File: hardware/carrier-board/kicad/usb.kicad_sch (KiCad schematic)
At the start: 0 parts

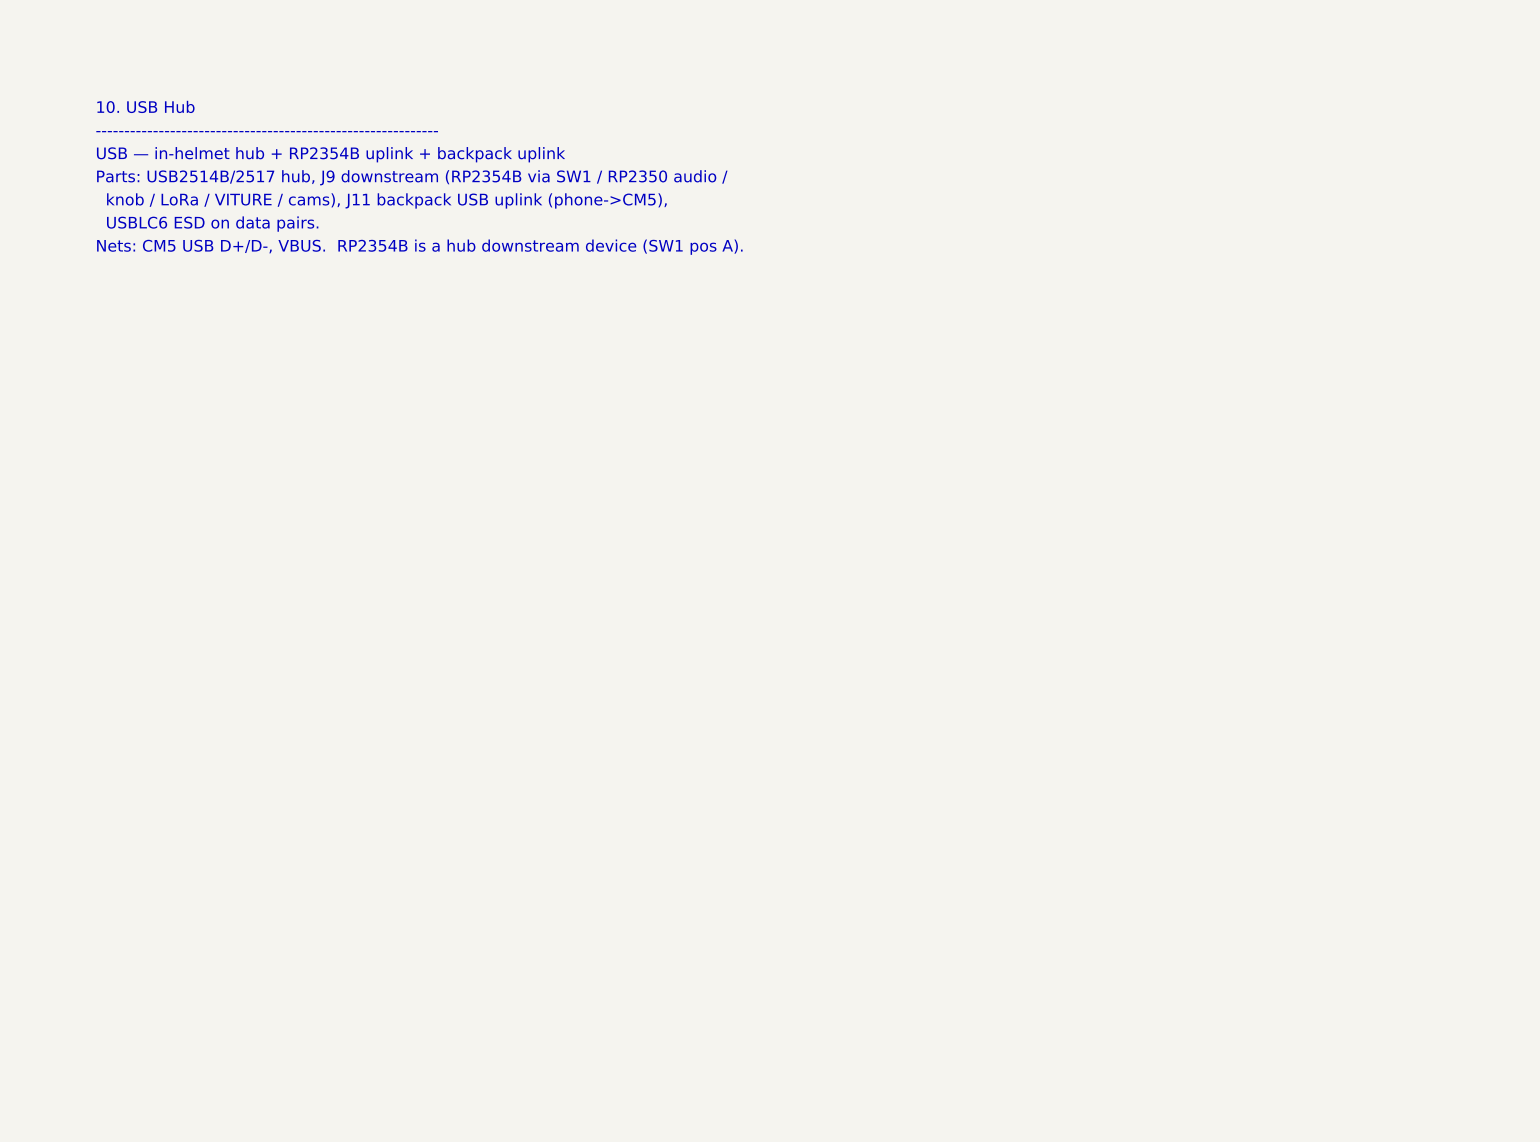
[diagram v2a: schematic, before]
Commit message: Carrier KiCad: populate all 11 schematic sheets
Replace populate_face_buffer.py with populate_sheets.py: one generator that
emits all 11 populated sub-sheets reusing the KiCad-9 format proven by the
face_buffer proof. Shared symbol library + generic box-symbol builder; condensed
CM5 (2x DF40-100) and RP2354B (QFN-80) symbols showing only used pins.

Connectivity by net labels (global for rails + cross-sheet nets: GPIOxx HUB75,
MX_*, LED*_DAT, SRV*, BTN*, *_USB_*; local within-sheet). Sheets: power
(protection + rails + AP2112 +3V3_RP), cm5 (HUB75 out + fan MOSFETs + RP ctrl),
face_buffer, rp2354_io (RP2354B + xtal + SW1/J12 + ESD + SWD), rp2354_face
(U10->J3), leds (U11 quad ->J4a-d), sensors_i2c (pull-ups+J5+STEMMA),
servos (J20-27 + rail), gpio_buttons (J6), usb (USB2514B hub + uplink),
cameras_display (CSI FFC + HDMI).

Verified: all sheets paren-balanced, every used lib_id defined, all instance
paths match sheet UUIDs, root<->sub-sheet UUID linkage intact. generate_skeleton.py
now lists all sheets POPULATED (writes only root+project). Not yet opened in
KiCad here -- expect ERC warnings (PWR_FLAG, unconnected pins) to clean.
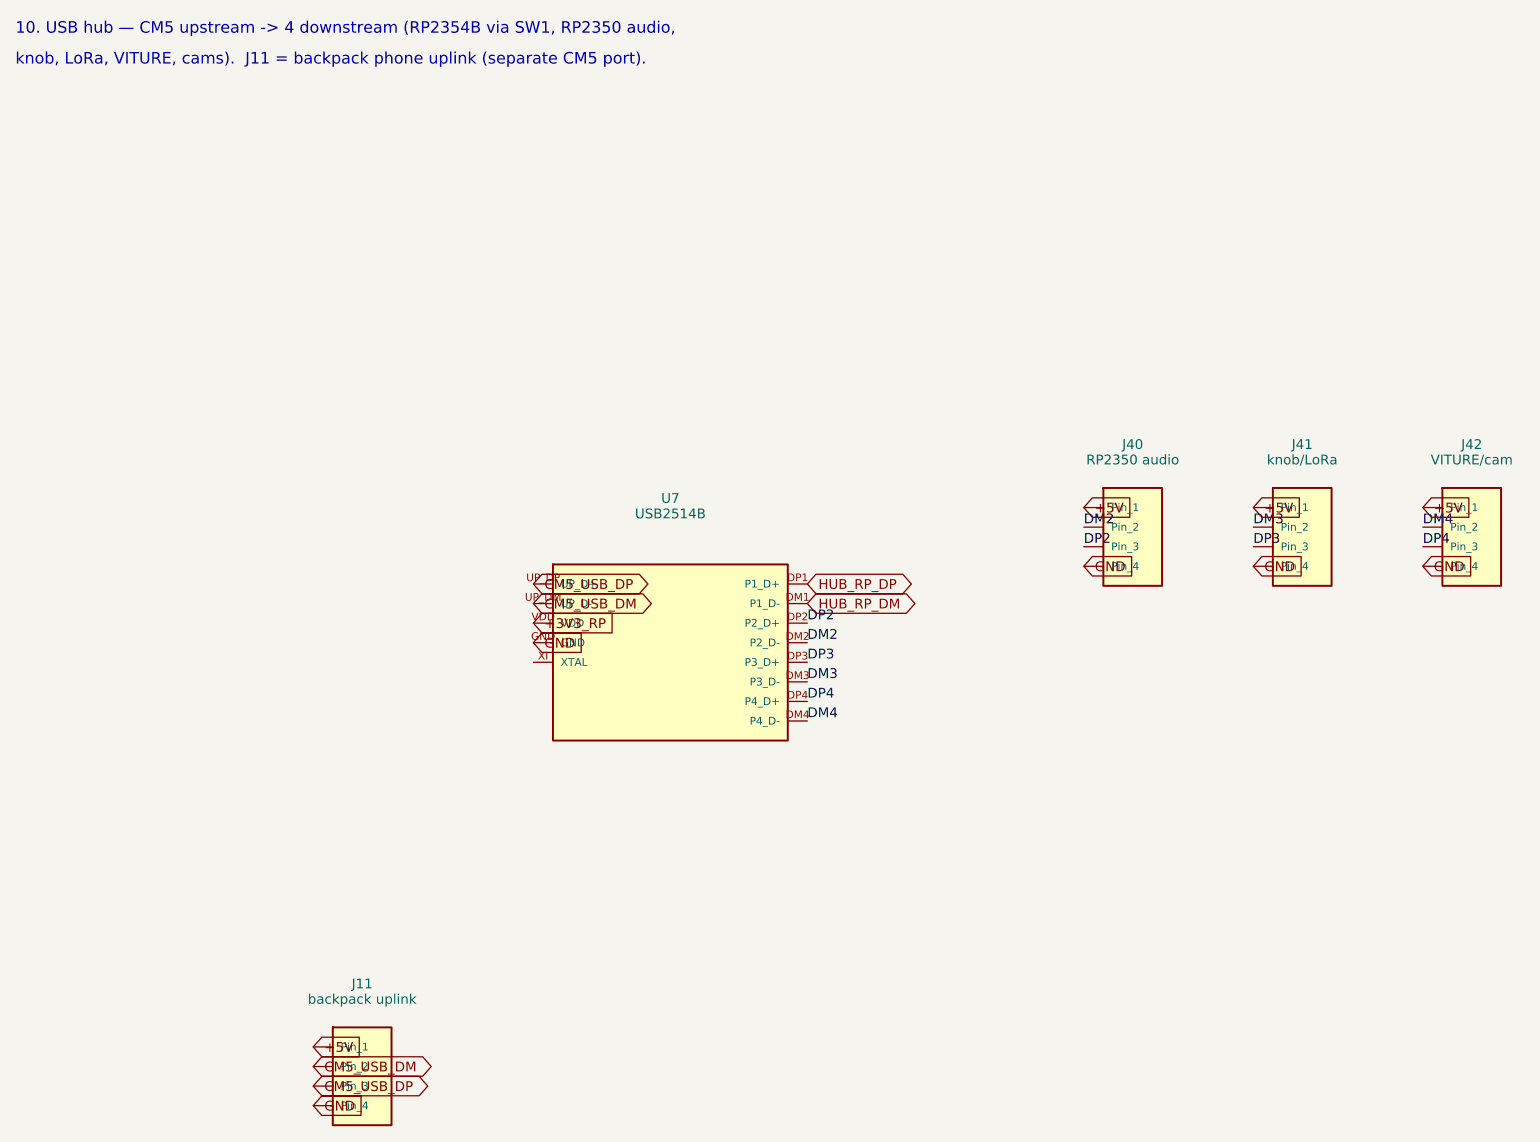
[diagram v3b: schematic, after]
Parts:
- added J11: backpack uplink, symbol Connector_Generic:Conn_01x04
- added J40: RP2350 audio, symbol Connector_Generic:Conn_01x04
- added J41: knob/LoRa, symbol Connector_Generic:Conn_01x04
- added J42: VITURE/cam, symbol Connector_Generic:Conn_01x04
- added U7: USB2514B, symbol Interface_USB:USB2514B
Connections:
- new net +3V3_RP: U7.VDD
- new net +5V: J11.1 (Pin_1), J40.1 (Pin_1), J41.1 (Pin_1), J42.1 (Pin_1)
- new net CM5_USB_DM: J11.2 (Pin_2), U7.UP_DM (UP_D-)
- new net CM5_USB_DP: J11.3 (Pin_3), U7.UP_DP (UP_D+)
- new net DM2: J40.2 (Pin_2), U7.DM2 (P2_D-)
- new net DM3: J41.2 (Pin_2), U7.DM3 (P3_D-)
- new net DM4: J42.2 (Pin_2), U7.DM4 (P4_D-)
- new net DP2: J40.3 (Pin_3), U7.DP2 (P2_D+)
- new net DP3: J41.3 (Pin_3), U7.DP3 (P3_D+)
- new net DP4: J42.3 (Pin_3), U7.DP4 (P4_D+)
- new net GND: J11.4 (Pin_4), J40.4 (Pin_4), J41.4 (Pin_4), J42.4 (Pin_4), U7.GND
- new net HUB_RP_DM: U7.DM1 (P1_D-)
- new net HUB_RP_DP: U7.DP1 (P1_D+)
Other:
- note added: "10. USB hub — CM5 upstream -> 4 downstream (RP2354B via SW1, RP2350 audio,"
- note added: "knob, LoRa, VITURE, cams). J11 = backpack phone uplink (separate CM5 port)."
- note removed: "------------------------------------------------------------"
- note removed: "10. USB Hub"
- note removed: "Nets: CM5 USB D+/D-, VBUS. RP2354B is a hub downstream device (SW1 pos A)."
- note removed: "Parts: USB2514B/2517 hub, J9 downstream (RP2354B via SW1 / RP2350 audio /"
- note removed: "USB — in-helmet hub + RP2354B uplink + backpack uplink"
- note removed: "USBLC6 ESD on data pairs."
- note removed: "knob / LoRa / VITURE / cams), J11 backpack USB uplink (phone->CM5),"
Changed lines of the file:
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@@
 (kicad_sch
-  (version 20230121)
-  (generator protohud_skeleton)
+  (version 20250114)
+  (generator "protohud_populate")
+  (generator_version "9.0")
   (paper "A3")
   (title_block
@@
     (company "ProtoHUD")
   )
-  (text "10. USB Hub" (at 25.4 25.40 0) (effects (font (size 1.5 1.5)) (justify left bottom)))
-  (text "------------------------------------------------------------" (at 25.4 28.40 0) (effects (font (size 1.5 1.5)) (justify left bottom)))
-  (text "USB — in-helmet hub + RP2354B uplink + backpack uplink" (at 25.4 31.40 0) (effects (font (size 1.5 1.5)) (justify left bottom)))
-  (text "Parts: USB2514B/2517 hub, J9 downstream (RP2354B via SW1 / RP2350 audio /" (at 25.4 34.40 0) (effects (font (size 1.5 1.5)) (justify left bottom)))
-  (text "  knob / LoRa / VITURE / cams), J11 backpack USB uplink (phone->CM5)," (at 25.4 37.40 0) (effects (font (size 1.5 1.5)) (justify left bottom)))
-  (text "  USBLC6 ESD on data pairs." (at 25.4 40.40 0) (effects (font (size 1.5 1.5)) (justify left bottom)))
-  (text "Nets: CM5 USB D+/D-, VBUS.  RP2354B is a hub downstream device (SW1 pos A)." (at 25.4 43.40 0) (effects (font (size 1.5 1.5)) (justify left bottom)))
+  (text "10. USB hub — CM5 upstream -> 4 downstream (RP2354B via SW1, RP2350 audio," (at 15 15.0 0) (effects (font (size 1.5 1.5)) (justify left bottom)))
+  (text "knob, LoRa, VITURE, cams).  J11 = backpack phone uplink (separate CM5 port)." (at 15 19.0 0) (effects (font (size 1.5 1.5)) (justify left bottom)))
+  (symbol
+    (lib_id "Interface_USB:USB2514B")
+    (at 100.00 95.00 0)
+    (unit 1)
+    (exclude_from_sim no) (in_bom yes) (on_board yes) (dnp no)
+    (property "Reference" "U7" (at 100.00 75.00 0) (effects (font (size 1.27 1.27))))
+    (property "Value" "USB2514B" (at 100.00 77.00 0) (effects (font (size 1.27 1.27))))
+    (property "Footprint" "" (at 100.00 95.00 0) (effects (font (size 1.27 1.27)) (hide yes)))
+    (property "Datasheet" "" (at 100.00 95.00 0) (effects (font (size 1.27 1.27)) (hide yes)))
+    (pin "UP_DP")
+    (pin "UP_DM")
+    (pin "VDD")
+    (pin "GND")
+    (pin "XI")
+    (pin "DP1")
+    (pin "DM1")
+    (pin "DP2")
+    (pin "DM2")
+    (pin "DP3")
+    (pin "DM3")
+    (pin "DP4")
+    (pin "DM4")
+    (instances
+      (project "ProtoHUD-Carrier"
+        (path "/b12d177a-080c-49c4-8372-6cdd7e6e9f72"
+          (reference "U7") (unit 1))))
+  )
+  (symbol
+    (lib_id "Connector_Generic:Conn_01x04")
+    (at 160.00 80.00 0)
+    (unit 1)
+    (exclude_from_sim no) (in_bom yes) (on_board yes) (dnp no)
+    (property "Reference" "J40" (at 160.00 68.00 0) (effects (font (size 1.27 1.27))))
+    (property "Value" "RP2350 audio" (at 160.00 70.00 0) (effects (font (size 1.27 1.27))))
+    (property "Footprint" "" (at 160.00 80.00 0) (effects (font (size 1.27 1.27)) (hide yes)))
+    (property "Datasheet" "" (at 160.00 80.00 0) (effects (font (size 1.27 1.27)) (hide yes)))
+    (pin "1")
+    (pin "2")
+    (pin "3")
+    (pin "4")
+    (instances
+      (project "ProtoHUD-Carrier"
+        (path "/b12d177a-080c-49c4-8372-6cdd7e6e9f72"
+          (reference "J40") (unit 1))))
+  )
+  (symbol
+    (lib_id "Connector_Generic:Conn_01x04")
+    (at 182.00 80.00 0)
+    (unit 1)
+    (exclude_from_sim no) (in_bom yes) (on_board yes) (dnp no)
+    (property "Reference" "J41" (at 182.00 68.00 0) (effects (font (size 1.27 1.27))))
+    (property "Value" "knob/LoRa" (at 182.00 70.00 0) (effects (font (size 1.27 1.27))))
+    (property "Footprint" "" (at 182.00 80.00 0) (effects (font (size 1.27 1.27)) (hide yes)))
+    (property "Datasheet" "" (at 182.00 80.00 0) (effects (font (size 1.27 1.27)) (hide yes)))
+    (pin "1")
+    (pin "2")
+    (pin "3")
+    (pin "4")
+    (instances
+      (project "ProtoHUD-Carrier"
+        (path "/b12d177a-080c-49c4-8372-6cdd7e6e9f72"
+          (reference "J41") (unit 1))))
+  )
+  (symbol
+    (lib_id "Connector_Generic:Conn_01x04")
+    (at 204.00 80.00 0)
+    (unit 1)
+    (exclude_from_sim no) (in_bom yes) (on_board yes) (dnp no)
+    (property "Reference" "J42" (at 204.00 68.00 0) (effects (font (size 1.27 1.27))))
+    (property "Value" "VITURE/cam" (at 204.00 70.00 0) (effects (font (size 1.27 1.27))))
+    (property "Footprint" "" (at 204.00 80.00 0) (effects (font (size 1.27 1.27)) (hide yes)))
+    (property "Datasheet" "" (at 204.00 80.00 0) (effects (font (size 1.27 1.27)) (hide yes)))
+    (pin "1")
+    (pin "2")
+    (pin "3")
+    (pin "4")
+    (instances
+      (project "ProtoHUD-Carrier"
+        (path "/b12d177a-080c-49c4-8372-6cdd7e6e9f72"
+          (reference "J42") (unit 1))))
+  )
+  (symbol
+    (lib_id "Connector_Generic:Conn_01x04")
+    (at 60.00 150.00 0)
+    (unit 1)
+    (exclude_from_sim no) (in_bom yes) (on_board yes) (dnp no)
+    (property "Reference" "J11" (at 60.00 138.00 0) (effects (font (size 1.27 1.27))))
+    (property "Value" "backpack uplink" (at 60.00 140.00 0) (effects (font (size 1.27 1.27))))
+    (property "Footprint" "" (at 60.00 150.00 0) (effects (font (size 1.27 1.27)) (hide yes)))
+    (property "Datasheet" "" (at 60.00 150.00 0) (effects (font (size 1.27 1.27)) (hide yes)))
+    (pin "1")
+    (pin "2")
+    (pin "3")
+    (pin "4")
+    (instances
+      (project "ProtoHUD-Carrier"
+        (path "/b12d177a-080c-49c4-8372-6cdd7e6e9f72"
+          (reference "J11") (unit 1))))
+  )
+  (global_label "+3V3_RP" (shape input) (at 82.22 91.19 180) (effects (font (size 1.27 1.27)) (justify left)))
+  (global_label "GND" (shape input) (at 82.22 93.73 180) (effects (font (size 1.27 1.27)) (justify left)))
+  (global_label "CM5_USB_DP" (shape bidirectional) (at 82.22 86.11 180) (effects (font (size 1.27 1.27)) (justify left)))
+  (global_label "CM5_USB_DM" (shape bidirectional) (at 82.22 88.65 180) (effects (font (size 1.27 1.27)) (justify left)))
+  (global_label "HUB_RP_DP" (shape bidirectional) (at 117.78 86.11 0) (effects (font (size 1.27 1.27)) (justify left)))
+  (global_label "HUB_RP_DM" (shape bidirectional) (at 117.78 88.65 0) (effects (font (size 1.27 1.27)) (justify left)))
+  (global_label "+5V" (shape input) (at 153.65 76.19 180) (effects (font (size 1.27 1.27)) (justify left)))
+  (label "DM2" (at 153.65 78.73 180) (effects (font (size 1.27 1.27)) (justify left bottom)))
+  (label "DP2" (at 153.65 81.27 180) (effects (font (size 1.27 1.27)) (justify left bottom)))
+  (global_label "GND" (shape input) (at 153.65 83.81 180) (effects (font (size 1.27 1.27)) (justify left)))
+  (label "DP2" (at 117.78 91.19 0) (effects (font (size 1.27 1.27)) (justify left bottom)))
+  (label "DM2" (at 117.78 93.73 0) (effects (font (size 1.27 1.27)) (justify left bottom)))
+  (global_label "+5V" (shape input) (at 175.65 76.19 180) (effects (font (size 1.27 1.27)) (justify left)))
+  (label "DM3" (at 175.65 78.73 180) (effects (font (size 1.27 1.27)) (justify left bottom)))
+  (label "DP3" (at 175.65 81.27 180) (effects (font (size 1.27 1.27)) (justify left bottom)))
+  (global_label "GND" (shape input) (at 175.65 83.81 180) (effects (font (size 1.27 1.27)) (justify left)))
+  (label "DP3" (at 117.78 96.27 0) (effects (font (size 1.27 1.27)) (justify left bottom)))
+  (label "DM3" (at 117.78 98.81 0) (effects (font (size 1.27 1.27)) (justify left bottom)))
+  (global_label "+5V" (shape input) (at 197.65 76.19 180) (effects (font (size 1.27 1.27)) (justify left)))
+  (label "DM4" (at 197.65 78.73 180) (effects (font (size 1.27 1.27)) (justify left bottom)))
+  (label "DP4" (at 197.65 81.27 180) (effects (font (size 1.27 1.27)) (justify left bottom)))
+  (global_label "GND" (shape input) (at 197.65 83.81 180) (effects (font (size 1.27 1.27)) (justify left)))
+  (label "DP4" (at 117.78 101.35 0) (effects (font (size 1.27 1.27)) (justify left bottom)))
+  (label "DM4" (at 117.78 103.89 0) (effects (font (size 1.27 1.27)) (justify left bottom)))
+  (global_label "+5V" (shape input) (at 53.65 146.19 180) (effects (font (size 1.27 1.27)) (justify left)))
+  (global_label "CM5_USB_DM" (shape bidirectional) (at 53.65 148.73 180) (effects (font (size 1.27 1.27)) (justify left)))
+  (global_label "CM5_USB_DP" (shape bidirectional) (at 53.65 151.27 180) (effects (font (size 1.27 1.27)) (justify left)))
+  (global_label "GND" (shape input) (at 53.65 153.81 180) (effects (font (size 1.27 1.27)) (justify left)))
   (sheet_instances
     (path "/" (page "1"))
